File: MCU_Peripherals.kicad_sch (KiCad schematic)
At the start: 36 parts, among them J1 USB_C_Receptacle_USB2.0_16P, J2 Conn_01x02_Socket, J3 Conn_01x04_Pin, J6 Conn_01x02_Socket, U2 SN65HVD230DR, U3 USBLC6-2SC6, U4 M24C64-RMN6TP, Y1 Crystal_16MHz

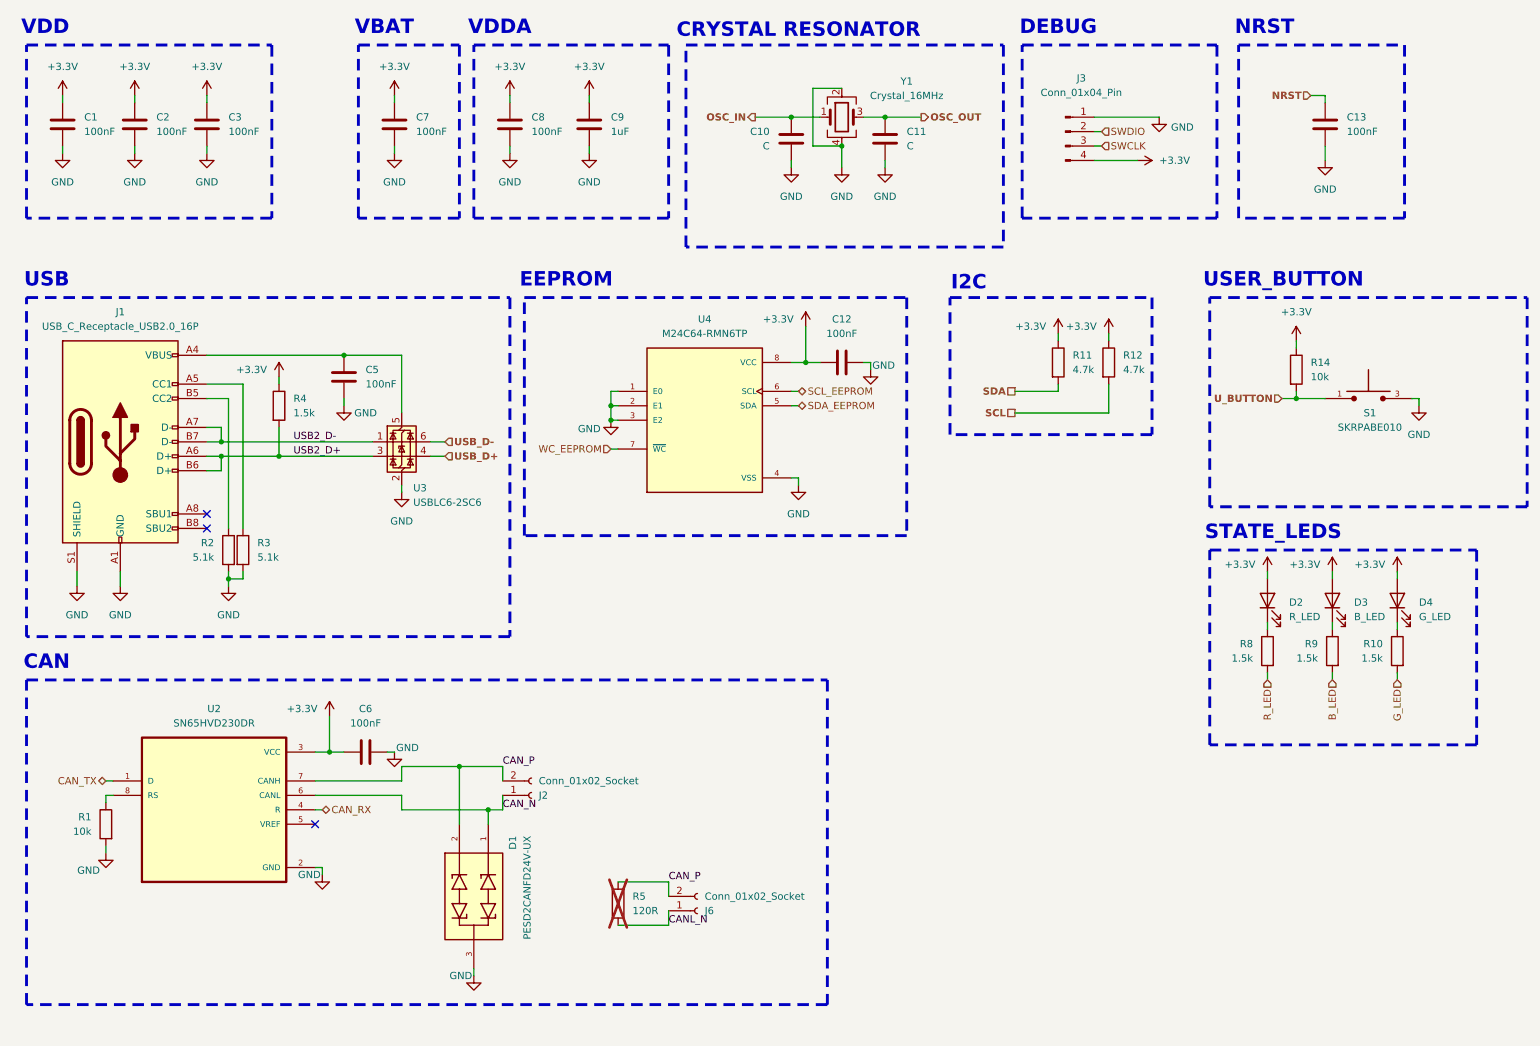
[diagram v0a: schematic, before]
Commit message: Schematic check, Text adjustment & QoL changes
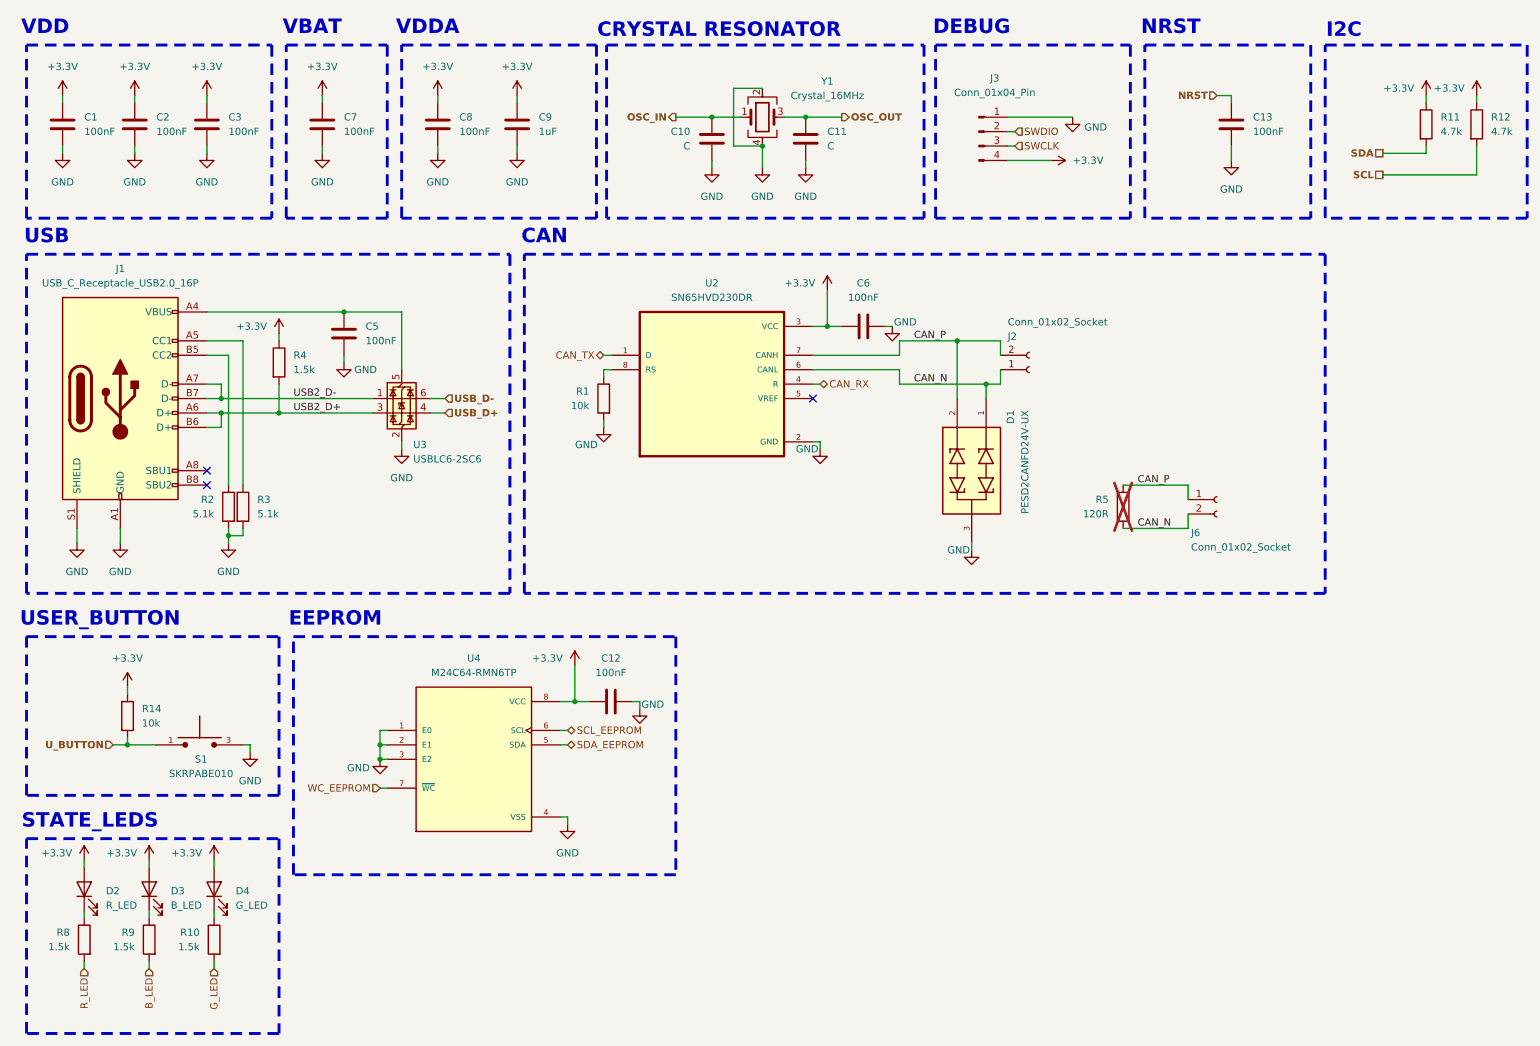
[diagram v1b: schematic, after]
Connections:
- net CAN_N: now also J6.2 (Pin_2), R5.2
- net CAN_P: now also J6.1 (Pin_1); no longer J6.2 (Pin_2)
- removed net CANL_N: J6.1 (Pin_1), R5.2
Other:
- moved on the sheet: C10, C11, C12, C13, C5, C6, C7, C8, C9, D1, D2, D3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

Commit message: Constrains & Check
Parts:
- C10, C11: value C -> 30pF; footprint Capacitor_SMD:C_0402_1005Metric_Pad0.74x0.62mm_HandSolder -> Capacitor_SMD:C_0603_1608Metric_Pad1.08x0.95mm_HandSolder
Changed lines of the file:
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@@
 			)
 		)
-		(property "Value" "C"
+		(property "Value" "30pF"
 			(at 156.21 36.8299 0)
 			(effects
@@
 			)
 		)
-		(property "Footprint" "Capacitor_SMD:C_0402_1005Metric_Pad0.74x0.62mm_HandSolder"
+		(property "Footprint" "Capacitor_SMD:C_0603_1608Metric_Pad1.08x0.95mm_HandSolder"
 			(at 153.3652 39.37 0)
 			(effects
@@
 			)
 		)
-		(property "Value" "C"
+		(property "Value" "30pF"
 			(at 132.08 36.8299 0)
 			(effects
@@
 			)
 		)
-		(property "Footprint" "Capacitor_SMD:C_0402_1005Metric_Pad0.74x0.62mm_HandSolder"
+		(property "Footprint" "Capacitor_SMD:C_0603_1608Metric_Pad1.08x0.95mm_HandSolder"
 			(at 134.9248 39.37 0)
 			(effects
